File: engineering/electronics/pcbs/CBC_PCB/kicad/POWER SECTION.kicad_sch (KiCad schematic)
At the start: 99 parts, among them J4 AMT0650009DB0000G, J5 AMT0650009DB0000G, J6 AMT0650009DB0000G, J7 AMT0650009DB0000G, Q4 SP015N03BGHTO, U10 CPC1106NTR, U11 CPC1106NTR, U12 74LVC1G17W5-7, U13 74LVC2G02HK3-7, U14 MAX810R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

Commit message: electronics: integrate CBC PCB updates
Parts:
- added F2, F3: (no value), EasyEDA_Lib:FUSE-SMD_L9.8-W5.1, symbol CBC_PCB:0154001.DR
- added LED2, LED3, LED4: (no value), EasyEDA_Lib:LED0603-RD, symbol CBC_PCB:0603 Green 509-620mcd
- added R63, R64, R65: 1.8kΩ, EasyEDA_Lib:R0603, symbol CBC_PCB:0603WAF1801T5E
- C105, C106, C81, C82, C83, C89, C90, C91: symbol EasyEDA_Lib:CL21A475KBQNNNE -> CBC_PCB:CL21A475KBQNNNE
- C107, C36, C80, C84, C87, C88, C92: symbol EasyEDA_Lib:CL10B104KC8NNNC -> CBC_PCB:CL10B104KC8NNNC
- C27, C28, C31: symbol EasyEDA_Lib:GRM21BR61H106KE43L -> CBC_PCB:GRM21BR61H106KE43L
- C78, C79, C85, C86: symbol EasyEDA_Lib:ERJ1KM2R2D11OT -> CBC_PCB:ERJ1KM2R2D11OT
- CN2: symbol EasyEDA_Lib:A1257WV-S-2P -> CBC_PCB:A1257WV-S-2P
- D10, D11, D12, D13, D22, D23, D6, D8: symbol EasyEDA_Lib:SMBJ13CA_C19077568 -> CBC_PCB:SMBJ13CA_C19077568
- D24, D26: symbol EasyEDA_Lib:FSV10150V -> CBC_PCB:FSV10150V
- D25, D27: symbol EasyEDA_Lib:SMBJ5.0CA_C83323 -> CBC_PCB:SMBJ5.0CA_C83323
- D7: symbol EasyEDA_Lib:SMBJ78CA_C2903953 -> CBC_PCB:SMBJ78CA_C2903953
- D9: symbol EasyEDA_Lib:ES3D_C241735 -> CBC_PCB:ES3D_C241735
- F1: symbol EasyEDA_Lib:0154005.DR -> CBC_PCB:0154005.DR
- HC1, HC3: footprint C90D_PAD:C90D_PAD -> CBC_PCB:C90D_PAD; symbol C90D_PAD:C90D_PAD -> CBC_PCB:C90D_PAD
- J4, J5, J6, J7: symbol AMT0650009DB0000G:AMT0650009DB0000G -> CBC_PCB:AMT0650009DB0000G
- L7, L8: symbol EasyEDA_Lib:ZEMS0850-330M -> CBC_PCB:ZEMS0850-330M
- Q10, Q11, Q2, Q3, Q4, Q5, Q6, Q7: symbol EasyEDA_Lib:SP015N03BGHTO -> CBC_PCB:SP015N03BGHTO
- R12, R16, R20, R24, R25, R26, R27, R28, R46, R47: symbol EasyEDA_Lib:RT0402BRD0710KL -> CBC_PCB:RT0402BRD0710KL
- R13: symbol EasyEDA_Lib:RT0603BRD07100KL -> CBC_PCB:RT0603BRD07100KL
- R14: symbol EasyEDA_Lib:RT0402BRD073K3L -> CBC_PCB:RT0402BRD073K3L
- R15, R23, R29: symbol EasyEDA_Lib:RC0402FR-07330RL -> CBC_PCB:RC0402FR-07330RL
- R21, R22: symbol EasyEDA_Lib:AC05000003309JAC00 -> CBC_PCB:AC05000003309JAC00
- R48, R53: symbol EasyEDA_Lib:25121WF100JT4E -> CBC_PCB:25121WF100JT4E
- R49, R54: footprint (none) -> EasyEDA_Lib:R0603
- R50, R52, R55, R57: symbol EasyEDA_Lib:RT0603BRD0710KL -> CBC_PCB:RT0603BRD0710KL
- R51, R56: symbol EasyEDA_Lib:PTFR0603B140KP9 -> CBC_PCB:PTFR0603B140KP9
- U10, U11: symbol EasyEDA_Lib:CPC1106NTR -> CBC_PCB:CPC1106NTR
- U12: symbol EasyEDA_Lib:74LVC1G17W5-7 -> CBC_PCB:74LVC1G17W5-7
- U13: symbol EasyEDA_Lib:74LVC2G02HK3-7 -> CBC_PCB:74LVC2G02HK3-7
- U14: symbol EasyEDA_Lib:MAX810R -> CBC_PCB:MAX810R
- U16, U17, U18, U19, U20, U21, U31, U32: symbol EasyEDA_Lib:MCS0402MC1001FE000 -> CBC_PCB:MCS0402MC1001FE000
- U22: symbol EasyEDA_Lib:CPC1019NTR -> CBC_PCB:CPC1019NTR
- U33, U34: symbol MP9486GN-Z:MP9486GN-Z -> CBC_PCB:MP9486GN-Z
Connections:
- net 12V_GATE_P1: now also F2.1; no longer D5.2 (A)
- net 12V_GATE_P2: now also F3.1; no longer D30.2 (A)
- net H_PWR-IN-: now also LED2.1 (K), LED3.1 (K), LED4.1 (K)
- net SWITCHED_GATE_V: now also R65.1
- new net: LED4.2 (A), R65.2
- new net: D5.2 (A), F2.2, R63.1
- new net: D30.2 (A), F3.2, R64.1
- new net: LED3.2 (A), R64.2
- new net: LED2.2 (A), R63.2
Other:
- moved on the sheet: D30, D5

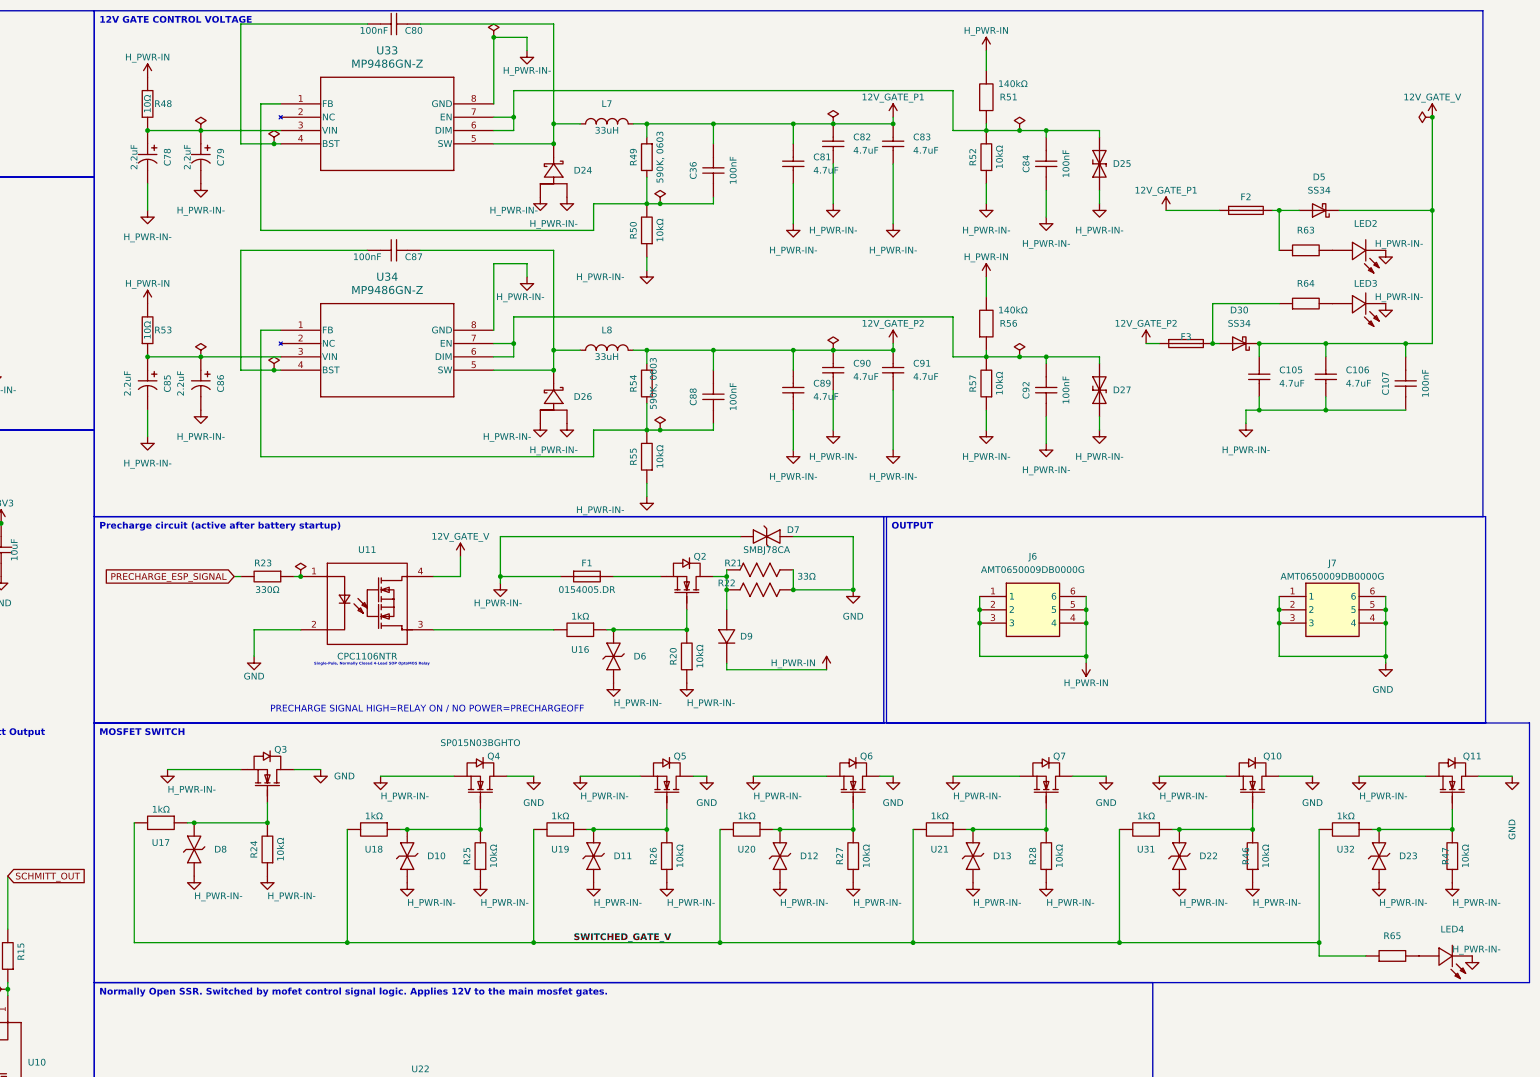
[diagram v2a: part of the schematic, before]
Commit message: electronics: update CMAIN and CBC PCB files
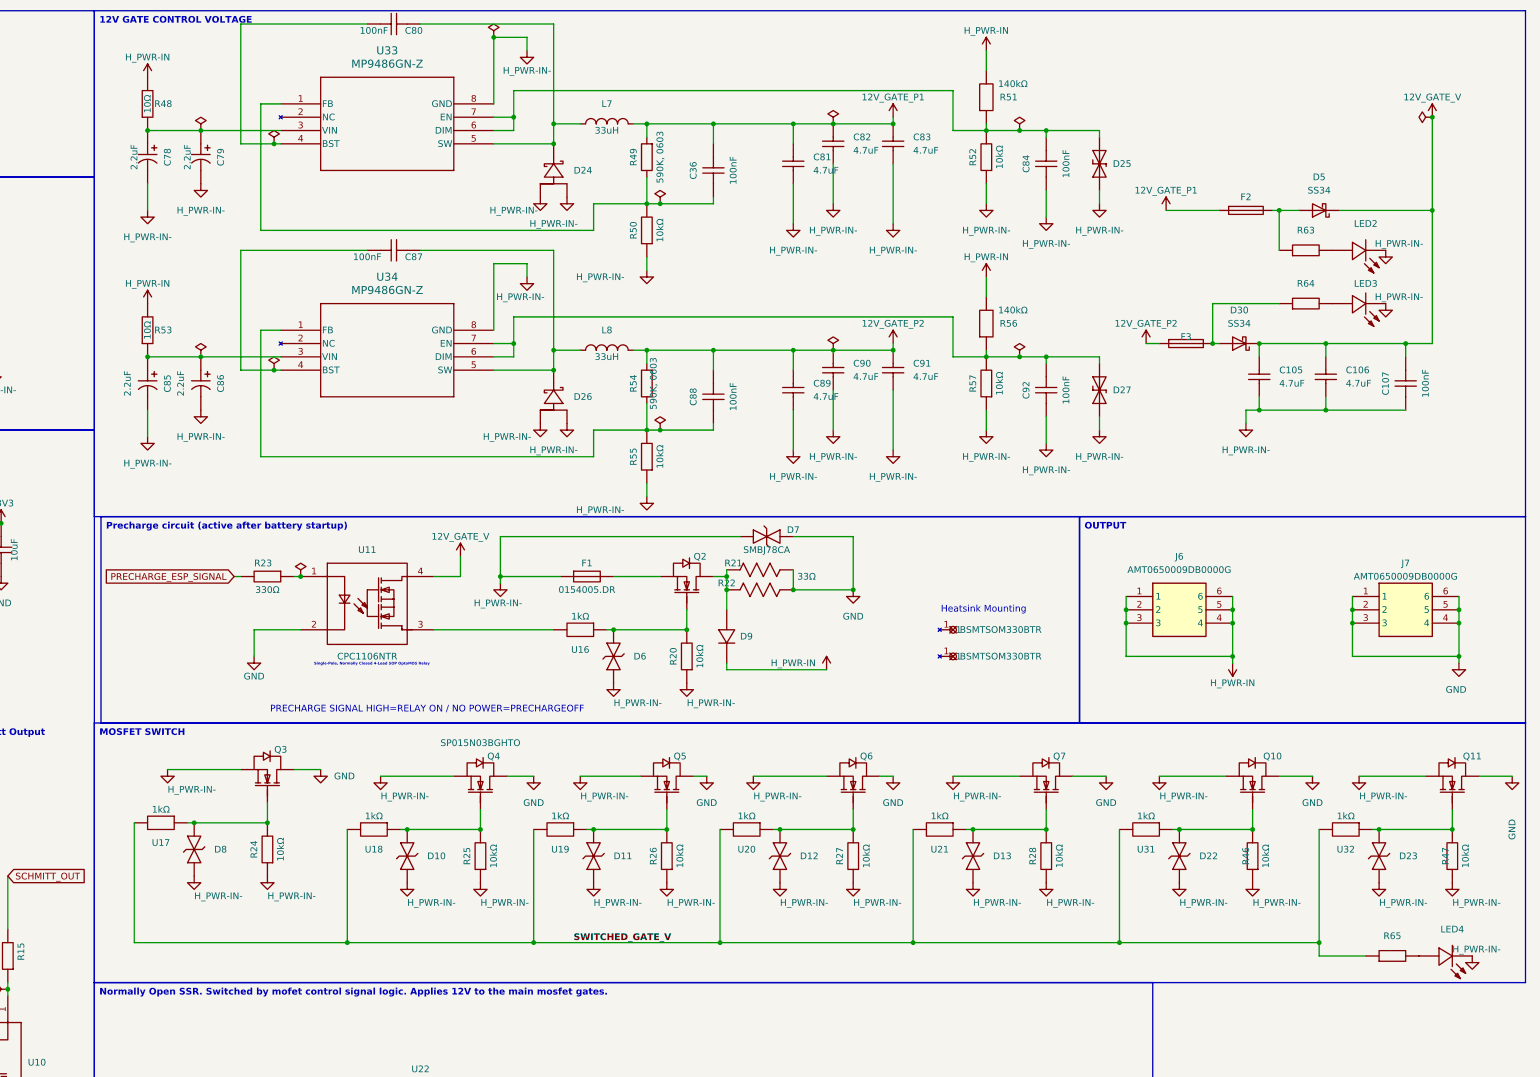
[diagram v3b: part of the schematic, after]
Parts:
- added U4, U40: BSMTSOM330BTR, CBC_PCB:SMD_BD6.0-D4.2, symbol CBC_PCB:SMTSOM380BTR
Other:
- note added: "Heatsink Mounting"
- moved on the sheet: J6, J7

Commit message: pcb: update CBC import and routing rules
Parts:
- removed U14: MAX810R, EasyEDA_Lib:SOT-23-3_L3.0-W1.6-P1.90-LS2.8-BR, symbol CBC_PCB:MAX810R
- added C108, C109: 100nF, EasyEDA_Lib:C0603, symbol CBC_PCB:CL10B104KC8NNNC
- added C21: 1uF, EasyEDA_Lib:C0805, symbol CBC_PCB:CC0805KKX7R0BB105
- added D31, D32: (no value), EasyEDA_Lib_2:SOD-323_L1.8-W1.3-LS2.5-RD, symbol EasyEDA_Lib_2:1N4148WS T4
- added R70: 10kΩ, EasyEDA_Lib_2:R0805, symbol EasyEDA_Lib_2:RC0805FR-0710KL
- added R71: 10kΩ, EasyEDA_Lib:R0402, symbol CBC_PCB:RT0402BRD0710KL
- C27: value 10uF -> 100uF; footprint EasyEDA_Lib:C0805 -> EasyEDA_Lib_2:CAP-SMD_BD6.3-L6.6-W6.6-LS7.4-FD; symbol CBC_PCB:GRM21BR61H106KE43L -> EasyEDA_Lib_2:A768EB107M1ELAS036; LCSC Part Name 10uF ±10% 50V -> 100uF ±20% 25V; Manufacturer muRata(村田) -> KEMET(基美); Manufacturer Part GRM21BR61H106KE43L -> A768EB107M1ELAS036; Supplier Part C440198 -> C1517616
- C78, C79, C85, C86: footprint EasyEDA_Lib:CAP-TH_BD5.0-P2.00-D0.5-FD-1 -> EasyEDA_Lib_2:C2220; symbol CBC_PCB:ERJ1KM2R2D11OT -> EasyEDA_Lib_2:FS55X225K251EGG; LCSC Part Name 2.2uF ±20% 100V -> 2.2uF ±10% 250V; Manufacturer AISHI(艾华集团) -> PSA(信昌电陶); Manufacturer Part ERJ1KM2R2D11OT -> FS55X225K251EGG; Supplier Part C694099 -> C153032
- D24, D26: footprint EasyEDA_Lib:TO-277A_L5.9-W4.4-LS6.5-TR -> EasyEDA_Lib_2:SMA_L4.3-W2.6-LS5.2-RD; symbol CBC_PCB:FSV10150V -> EasyEDA_Lib_2:SS2150_C47779; LCSC Part Name 电压:150V 电流:10A -> 电压:150V 电流:2A; Manufacturer onsemi(安森美) -> MDD(辰达半导体); Manufacturer Part FSV10150V -> SS2150; Supplier Part C719814 -> C47779
- L7, L8: footprint EasyEDA_Lib:IND-SMD_L8.5-W8.0_SMS0850 -> EasyEDA_Lib_2:IND-SMD_L5.0-W5.0-P3.60_SMNR5040; symbol CBC_PCB:ZEMS0850-330M -> EasyEDA_Lib_2:SMNR5040-330MT; LCSC Part Name 33UH ±20% 6A 一体成型电感，合金电感，大电流，低阻抗 -> 33uH ±20% 1.3A; Manufacturer ZE(增益) -> SXN(顺翔诺); Manufacturer Part ZEMS0850-330M -> SMNR5040-330MT; Supplier Part C41438711 -> C9390
- R12: value 10kΩ -> 120kΩ; footprint EasyEDA_Lib:R0402 -> EasyEDA_Lib_2:R0805; symbol CBC_PCB:RT0402BRD0710KL -> EasyEDA_Lib_2:RC0805FR-07120KL; LCSC Part Name 薄膜电阻 10kΩ ±0.1% 62.5mW -> 厚膜电阻 120kΩ ±1% 125mW; Manufacturer Part RT0402BRD0710KL -> RC0805FR-07120KL; Supplier Part C190095 -> C114524
- R13: value 100kΩ -> 15kΩ; footprint EasyEDA_Lib:R0603 -> EasyEDA_Lib_2:R0805; symbol CBC_PCB:RT0603BRD07100KL -> EasyEDA_Lib_2:RC0805FR-0715KL; LCSC Part Name 薄膜电阻 100kΩ ±0.1% 100mW -> 厚膜电阻 15kΩ ±1% 125mW; Manufacturer Part RT0603BRD07100KL -> RC0805FR-0715KL; Supplier Part C122538 -> C114559
- R14: value 3.3kΩ -> 36kΩ; footprint EasyEDA_Lib:R0402 -> EasyEDA_Lib_2:R0805; symbol CBC_PCB:RT0402BRD073K3L -> EasyEDA_Lib_2:RC0805FR-0736KL; LCSC Part Name 薄膜电阻 3.3kΩ ±0.1% 62.5mW -> 厚膜电阻 36kΩ ±1% 125mW; Manufacturer Part RT0402BRD073K3L -> RC0805FR-0736KL; Supplier Part C852763 -> C114527
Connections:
- net +3V3: now also C21.2
- net GND: now also C27.2, D32.2 (A), R70.1, R71.1; no longer C27.1
- net H_PWR-IN-: now also C78.1, C79.1, C85.1, C86.1, C108.2, C109.2; no longer C78.2, C79.2, C85.2, C86.2, D24.1 (A), D26.1 (A)
- net MOSFET_CONTROL_SIGNAL: now also R71.2
- net OUTPUT: now also C27.1; no longer C27.2
- net at R53.1, U34.3 (VIN): now also C85.2, C86.2, C109.1; no longer C85.1, C86.1
- net at C87.1, L8.1, U34.5 (SW): now also D26.1 (K); no longer D26.3 (K)
- net at C80.1, L7.1, U33.5 (SW): now also D24.1 (K); no longer D24.3 (K)
- net at R48.1, U33.3 (VIN): now also C78.2, C79.2, C108.1; no longer C78.1, C79.1
- net STARTUP_RESET: no longer names the net of U13.6 (2B)
- net STARTUP_RESET: now also D31.1 (K), R70.2
- new net: C21.1, D31.2 (A), D32.1 (K)
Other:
- note added: "STARTUP RESET PULSE"
- note removed: "5. Voltage at Every Node (Time vs Voltage) Time (sec) V_C1 Divider Node (to Schmitt) Schmitt Output 0.00 0.00V 0.00V LOW (0V) 0.25 2.65V 0.66V LOW 0.50 4.72V 1.17V LOW 0.75 6.27V 1.56V LOW 1.00 7.58V 1.88V LOW 1.25 8.69V 2.16V LOW 1.50 9.31V 2.31V → HIGH 1.75 9.79V 2.43V HIGH 2.00 10.38V 2.57V HIGH 2.50 11.04V 2.74V HIGH 3.00 11.40V 2.83V HIGH 4.00 11.80V 2.93V HIGH 5.00 11.92V 2.96V HIGH ∞ 12.00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"
- moved on the sheet: C31, R15, R16, R48, R53, U10, U13
